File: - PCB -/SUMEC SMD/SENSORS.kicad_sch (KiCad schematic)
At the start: 16 parts, among them U2 VL53L0X, U3 VL53L0X, U4 VL53L0X, U6 QRE1113, U7 QRE1113, U8 QRE1113, U9 QRE1113

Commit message: PCB SMD update
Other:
- title: SUMEC THT -> SUMEC SMD
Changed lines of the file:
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@@
   (paper "A4")
   (title_block
-    (title "SUMEC THT")
+    (title "SUMEC SMD")
     (company "SPŠ NA PROSEKU")
   )

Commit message: PCB Schematic SMD
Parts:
- R? (x8): footprint Resistor_THT:R_Axial_DIN0207_L6.3mm_D2.5mm_P10.16mm_Horizontal -> Resistor_SMD:R_1206_3216Metric
- U2, U3, U4: footprint sumec_library:GY-530 VL53L0X -> sumec-smd_library:GY-530 VL53L0X
- U6, U7, U8, U9: footprint sumec_library:OnSemi_CASE100AQ - QRE1113 -> sumec-smd_library:QRE1113GR-(smd)
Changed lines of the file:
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@@
       (effects (font (size 1.27 1.27)))
     )
-    (property "Footprint" "Resistor_THT:R_Axial_DIN0207_L6.3mm_D2.5mm_P10.16mm_Horizontal" (at 189.738 99.06 90)
+    (property "Footprint" "Resistor_SMD:R_1206_3216Metric" (at 189.738 99.06 90)
       (effects (font (size 1.27 1.27)) hide)
     )
@@
       (effects (font (size 1.27 1.27)))
     )
-    (property "Footprint" "Resistor_THT:R_Axial_DIN0207_L6.3mm_D2.5mm_P10.16mm_Horizontal" (at 241.808 129.54 90)
+    (property "Footprint" "Resistor_SMD:R_1206_3216Metric" (at 241.808 129.54 90)
       (effects (font (size 1.27 1.27)) hide)
     )
@@
       (effects (font (size 1 1)) (justify right))
     )
-    (property "Footprint" "sumec_library:GY-530 VL53L0X" (at 121.92 114.3 0)
+    (property "Footprint" "sumec-smd_library:GY-530 VL53L0X" (at 121.92 114.3 0)
       (effects (font (size 1.27 1.27)) hide)
     )
@@
       (effects (font (size 1.27 1.27)))
     )
-    (property "Footprint" "Resistor_THT:R_Axial_DIN0207_L6.3mm_D2.5mm_P10.16mm_Horizontal" (at 241.808 99.06 90)
+    (property "Footprint" "Resistor_SMD:R_1206_3216Metric" (at 241.808 99.06 90)
       (effects (font (size 1.27 1.27)) hide)
     )
@@
       (effects (font (size 1.27 1.27)))
     )
-    (property "Footprint" "Resistor_THT:R_Axial_DIN0207_L6.3mm_D2.5mm_P10.16mm_Horizontal" (at 189.738 129.54 90)
+    (property "Footprint" "Resistor_SMD:R_1206_3216Metric" (at 189.738 129.54 90)
       (effects (font (size 1.27 1.27)) hide)
     )
@@
       (effects (font (size 1.27 1.27)))
     )
-    (property "Footprint" "Resistor_THT:R_Axial_DIN0207_L6.3mm_D2.5mm_P10.16mm_Horizontal" (at 207.518 99.06 90)
+    (property "Footprint" "Resistor_SMD:R_1206_3216Metric" (at 207.518 99.06 90)
       (effects (font (size 1.27 1.27)) hide)
     )
@@
       (effects (font (size 1.27 1.27)) (justify left))
     )
-    (property "Footprint" "sumec_library:OnSemi_CASE100AQ - QRE1113" (at 180.34 110.49 0)
+    (property "Footprint" "sumec-smd_library:QRE1113GR-(smd)" (at 180.34 110.49 0)
       (effects (font (size 1.27 1.27)) hide)
     )
@@
       (effects (font (size 1.27 1.27)) (justify left))
     )
-    (property "Footprint" "sumec_library:OnSemi_CASE100AQ - QRE1113" (at 232.41 110.49 0)
+    (property "Footprint" "sumec-smd_library:QRE1113GR-(smd)" (at 232.41 110.49 0)
       (effects (font (size 1.27 1.27)) hide)
     )
@@
       (effects (font (size 1 1)) (justify right))
     )
-    (property "Footprint" "sumec_library:GY-530 VL53L0X" (at 48.26 114.3 0)
+    (property "Footprint" "sumec-smd_library:GY-530 VL53L0X" (at 48.26 114.3 0)
       (effects (font (size 1.27 1.27)) hide)
     )
@@
       (effects (font (size 1.27 1.27)))
     )
-    (property "Footprint" "Resistor_THT:R_Axial_DIN0207_L6.3mm_D2.5mm_P10.16mm_Horizontal" (at 225.298 129.54 90)
+    (property "Footprint" "Resistor_SMD:R_1206_3216Metric" (at 225.298 129.54 90)
       (effects (font (size 1.27 1.27)) hide)
     )
@@
       (effects (font (size 1.27 1.27)) (justify left))
     )
-    (property "Footprint" "sumec_library:OnSemi_CASE100AQ - QRE1113" (at 215.9 110.49 0)
+    (property "Footprint" "sumec-smd_library:QRE1113GR-(smd)" (at 215.9 110.49 0)
       (effects (font (size 1.27 1.27)) hide)
     )
@@
       (effects (font (size 1.27 1.27)))
     )
-    (property "Footprint" "Resistor_THT:R_Axial_DIN0207_L6.3mm_D2.5mm_P10.16mm_Horizontal" (at 207.518 129.54 90)
+    (property "Footprint" "Resistor_SMD:R_1206_3216Metric" (at 207.518 129.54 90)
       (effects (font (size 1.27 1.27)) hide)
     )
@@
       (effects (font (size 1 1)) (justify right))
     )
-    (property "Footprint" "sumec_library:GY-530 VL53L0X" (at 86.36 114.3 0)
+    (property "Footprint" "sumec-smd_library:GY-530 VL53L0X" (at 86.36 114.3 0)
       (effects (font (size 1.27 1.27)) hide)
     )
@@
       (effects (font (size 1.27 1.27)))
     )
-    (property "Footprint" "Resistor_THT:R_Axial_DIN0207_L6.3mm_D2.5mm_P10.16mm_Horizontal" (at 225.298 99.06 90)
+    (property "Footprint" "Resistor_SMD:R_1206_3216Metric" (at 225.298 99.06 90)
       (effects (font (size 1.27 1.27)) hide)
     )
@@
       (effects (font (size 1.27 1.27)) (justify left))
     )
-    (property "Footprint" "sumec_library:OnSemi_CASE100AQ - QRE1113" (at 198.12 110.49 0)
-      (effects (font (size 1.27 1.27)) hide)
-    )
+    (property "Footprint" "sumec-smd_library:QRE1113GR-(smd)" (at 198.12 110.49 0)
+      (effects (font (size 1.27 1.27)) hide)
+    )

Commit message: PCB SMD update
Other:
- moved on the sheet: R?, U6, U7, U8, U9

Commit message: PCB smd - schematic update
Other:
- note removed: "*potrebujeme GPIO?"
- moved on the sheet: R?, U2, U3, U4, U6, U7, U8, U9, U?

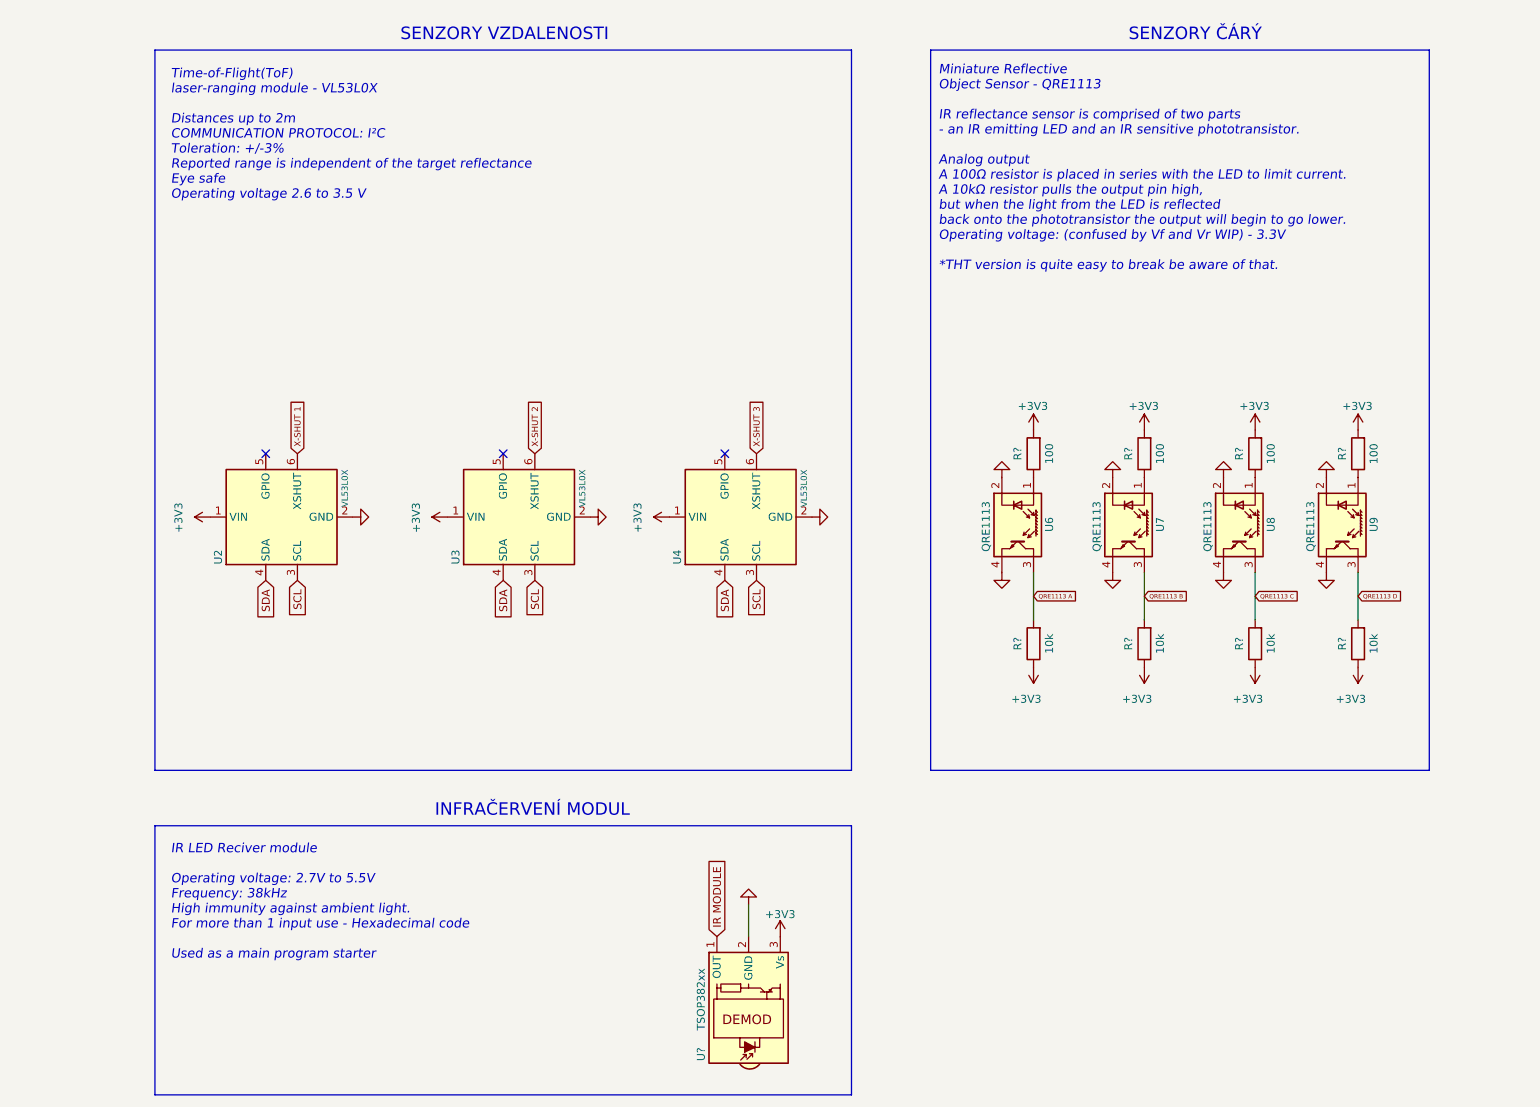
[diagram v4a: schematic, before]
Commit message: Custom Wheels update and PCB comp. naming update
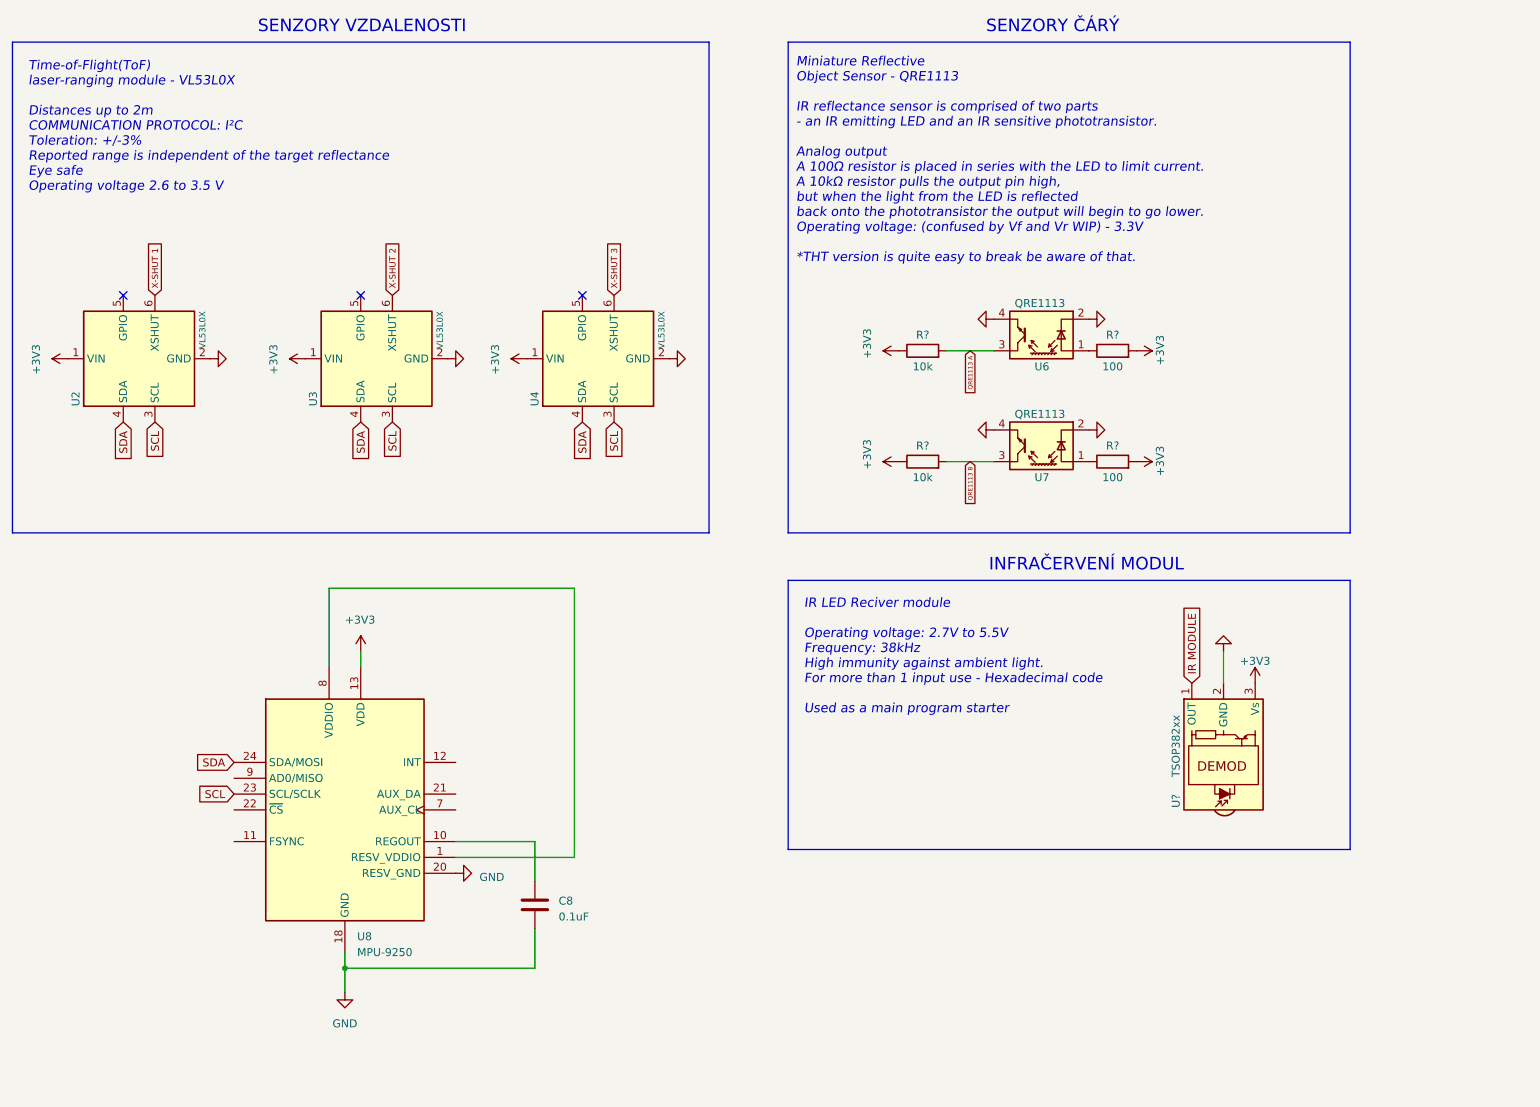
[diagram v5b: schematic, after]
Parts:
- removed R? (x2): 10k, Resistor_SMD:R_1206_3216Metric, symbol Device:R
- removed R? (x2): 100, Resistor_SMD:R_1206_3216Metric, symbol Device:R
- removed U8, U9: QRE1113, sumec-smd_library:QRE1113GR-(smd), symbol Sensor_Proximity:QRE1113
- added C8: 0.1uF, symbol Device:C
- added U8: MPU-9250, Sensor_Motion:InvenSense_QFN-24_3x3mm_P0.4mm, symbol Sensor_Motion:MPU-9250
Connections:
- net +3V3: now also U8.13 (VDD)
- net GND: now also C8.2, U8.18 (GND), U8.20 (RESV_GND)
- net SCL: now also U8.23 (SCL/SCLK)
- net SDA: now also U8.24 (SDA/MOSI)
- new net: U8.1 (RESV_VDDIO), U8.8 (VDDIO)
- new net: C8.1, U8.10 (REGOUT)
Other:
- moved on the sheet: R?, U2, U3, U4, U6, U7, U?

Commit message: PCB SMD - WIP ESP32 S3 WROOM 2
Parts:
- added R?: 100, Resistor_SMD:R_1206_3216Metric, symbol Device:R
- added R?: 10k, Resistor_SMD:R_1206_3216Metric, symbol Device:R
- added U13: QRE1113, sumec-smd_library:QRE1113GR-(smd), symbol Sensor_Proximity:QRE1113
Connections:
- net +3V3: now also R?.1, R?.2
- net GND: now also U13.2 (K), U13.4
- new net: R?.1, U13.1 (A)
- new net QRE1113 C: R?.2, U13.3
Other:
- note added: "Budeme použivat "LIDAR"?"
- note added: "WIP (later)"
- moved on the sheet: C8, R?, U6, U7, U8, U?

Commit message: pcb updae
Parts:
- added R?: 100, Resistor_SMD:R_1206_3216Metric, symbol Device:R
- added R?: 10k, Resistor_SMD:R_1206_3216Metric, symbol Device:R
- added U12: QRE1113, sumec-smd_library:QRE1113GR-(smd), symbol Sensor_Proximity:QRE1113
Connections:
- net +3V3: now also R?.1, R?.2
- net GND: now also U12.2 (K), U12.4
- new net: R?.1, U12.1 (A)
- new net QRE1113 D: R?.2, U12.3
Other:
- moved on the sheet: R?, U13, U2, U3, U4, U6, U7, U?

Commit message: PCB Update - "LIDAR"sensors
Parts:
- removed C8: 0.1uF, symbol Device:C
- removed U2, U3, U4: VL53L0X, sumec-smd_library:GY-530 VL53L0X, symbol sumec_library:GY-530_VL53L0X
- removed U8: MPU-9250, Sensor_Motion:InvenSense_QFN-24_3x3mm_P0.4mm, symbol Sensor_Motion:MPU-9250
- added J3 (x3): Conn_01x06_Pin, Connector_JST:JST_SHL_SM06B-SHLS-TF_1x06-1MP_P1.00mm_Horizontal, symbol Connector:Conn_01x06_Pin
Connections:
- net +3V3: now also J3.1 (Pin_1), J3.1 (Pin_1), J3.1 (Pin_1)
- net GND: now also J3.4 (Pin_4), J3.4 (Pin_4), J3.4 (Pin_4), J3.5 (Pin_5), J3.5 (Pin_5), J3.5 (Pin_5)
- net SCL: now also J3.3 (Pin_3), J3.3 (Pin_3), J3.3 (Pin_3)
- net SDA: now also J3.2 (Pin_2), J3.2 (Pin_2), J3.2 (Pin_2)
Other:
- note added: "Time-of-Flight(ToF) laser-ranging module - Distances up to COMMUNICATION PROTOCOL: I²C"
- note removed: "Budeme použivat "LIDAR"?"
- note removed: "Time-of-Flight(ToF) laser-ranging module - VL53L0X Distances up to 2m COMMUNICATION PROTOCOL: I²C Toleration: +/-3% Reported range is independent of the target reflectance Eye safe Operating voltage 2.6 to 3.5 V"
- note removed: "WIP (later)"
